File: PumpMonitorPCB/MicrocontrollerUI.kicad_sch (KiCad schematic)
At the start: 26 parts, among them J3 Debug, SW1 EN, SW2 BOOT, SW3 LEFT, SW4 RIGHT, U5 ESP32-S3-WROOM-1, U6 MC14504B

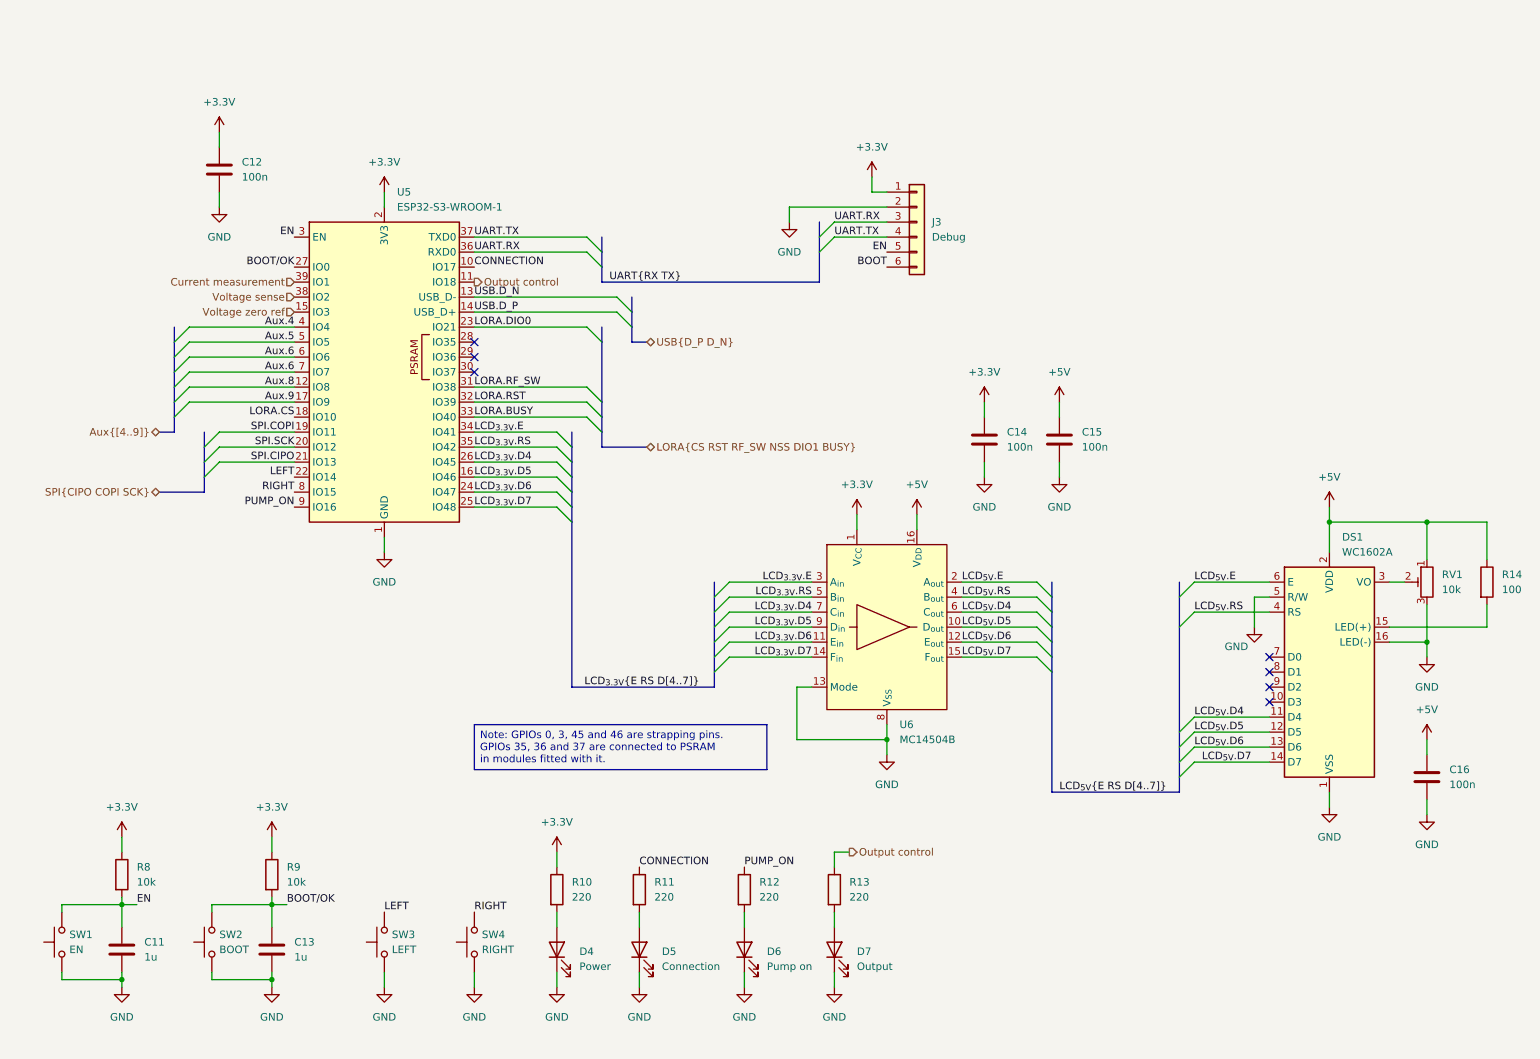
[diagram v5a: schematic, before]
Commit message: Rejigged auxilliary connectors, experimetning with kiclearance.
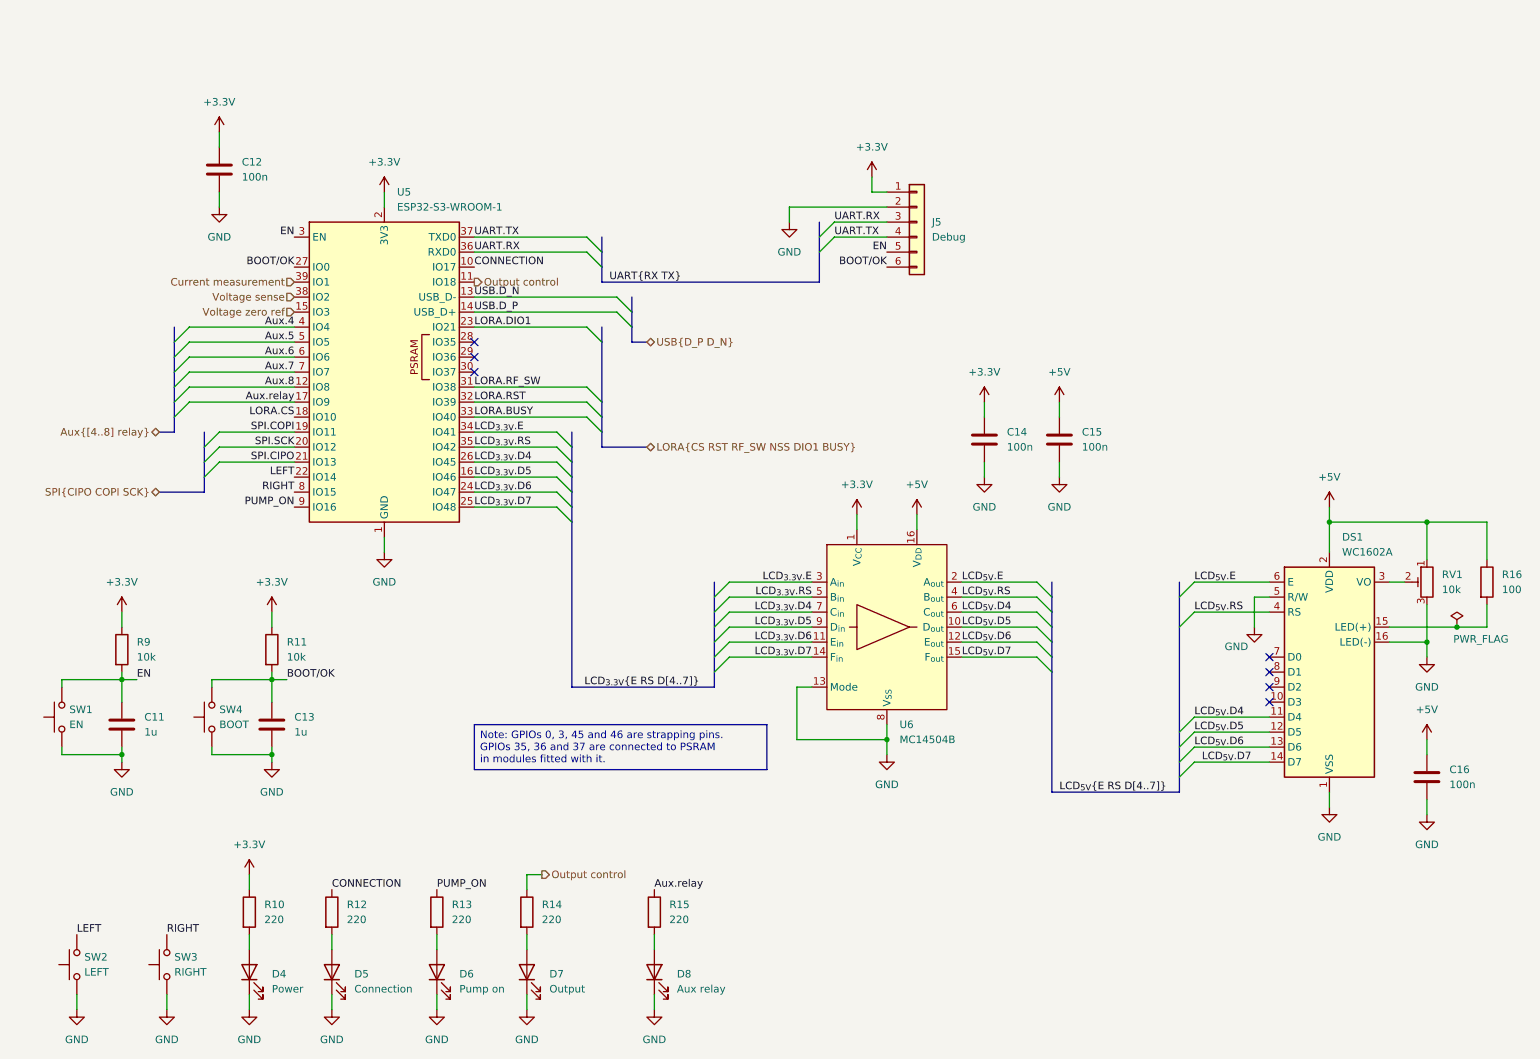
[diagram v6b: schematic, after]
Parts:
- added D8: Aux relay, LED_THT:LED_D5.0mm, symbol Device:LED
- added R15: 220, Resistor_SMD:R_0603_1608Metric_Pad0.98x0.95mm_HandSolder, symbol Device:R
- C11, C13: footprint Capacitor_SMD:C_0805_2012Metric_Pad1.18x1.45mm_HandSolder -> Capacitor_SMD:C_0603_1608Metric_Pad1.08x0.95mm_HandSolder; PlaceOnSecondary No -> (none)
- C12, C14, C15, C16: footprint Capacitor_SMD:C_0805_2012Metric_Pad1.18x1.45mm_HandSolder -> Capacitor_SMD:C_0603_1608Metric_Pad1.08x0.95mm_HandSolder
- R10: footprint Resistor_SMD:R_0805_2012Metric_Pad1.20x1.40mm_HandSolder -> Resistor_SMD:R_0603_1608Metric_Pad0.98x0.95mm_HandSolder
- R11: renamed from R9; PlaceOnSecondary No -> (none)
- R12: renamed from R11; footprint Resistor_SMD:R_0805_2012Metric_Pad1.20x1.40mm_HandSolder -> Resistor_SMD:R_0603_1608Metric_Pad0.98x0.95mm_HandSolder
- R13: renamed from R12; footprint Resistor_SMD:R_0805_2012Metric_Pad1.20x1.40mm_HandSolder -> Resistor_SMD:R_0603_1608Metric_Pad0.98x0.95mm_HandSolder
- R14: renamed from R13; footprint Resistor_SMD:R_0805_2012Metric_Pad1.20x1.40mm_HandSolder -> Resistor_SMD:R_0603_1608Metric_Pad0.98x0.95mm_HandSolder
- R16: renamed from R14; footprint Resistor_THT:R_Axial_DIN0207_L6.3mm_D2.5mm_P7.62mm_Horizontal -> Resistor_THT:R_Axial_DIN0309_L9.0mm_D3.2mm_P12.70mm_Horizontal
- R9: renamed from R8; PlaceOnSecondary No -> (none)
- SW1: PlaceOnSecondary No -> (none)
- SW2: renamed from SW3; PlaceOnSecondary No -> (none)
- SW3: renamed from SW4; PlaceOnSecondary No -> (none)
- SW4: renamed from SW2; PlaceOnSecondary No -> (none)
- renumbered J3 to J5
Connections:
- net BOOT is gone; now on net BOOT/OK: J5.6 (Pin_6)
- net Aux.6: no longer U5.7 (IO7)
- net GND: now also D8.1 (K)
- net Aux.9 renamed Aux.relay
- net Aux.relay: now also R15.1
- net LORA.DIO0 renamed LORA.DIO1
- new net: D8.2 (A), R15.2
- new net Aux.7: U5.7 (IO7)
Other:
- moved on the sheet: C11, C13, D4, D5, D6, D7, R10, R11, R12, R13, R14, R9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

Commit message: Adding test points, CAD files
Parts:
- C11, C13: DigikeyNumber (none) -> 587-1241-1-ND
- C12, C14, C15, C16: DigikeyNumber (none) -> 311-1088-1-ND
- DS1: footprint Display:WC1602A -> Connector_PinHeader_2.54mm:PinHeader_2x08_P2.54mm_Vertical
